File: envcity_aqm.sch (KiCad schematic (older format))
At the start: 9 parts, among them Q1 BSS138, Q2 BSS138, Q3 BSS138

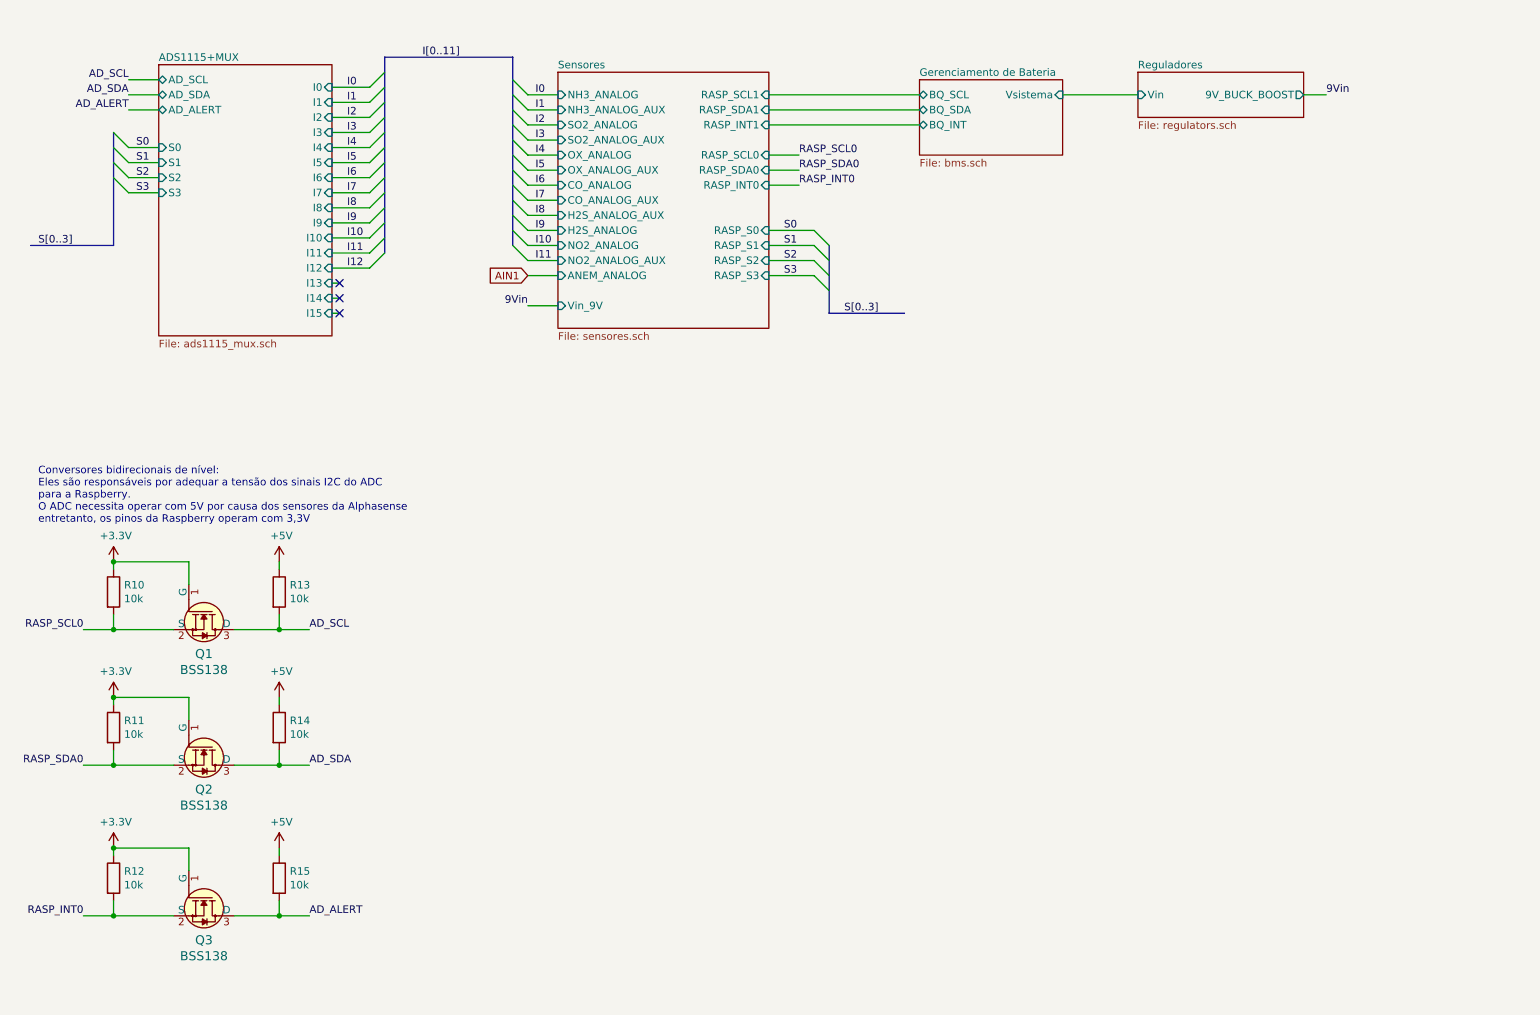
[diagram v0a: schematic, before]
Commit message: Adicionando radio LoRa. Criando um .sch para a Raspberry e para o radio
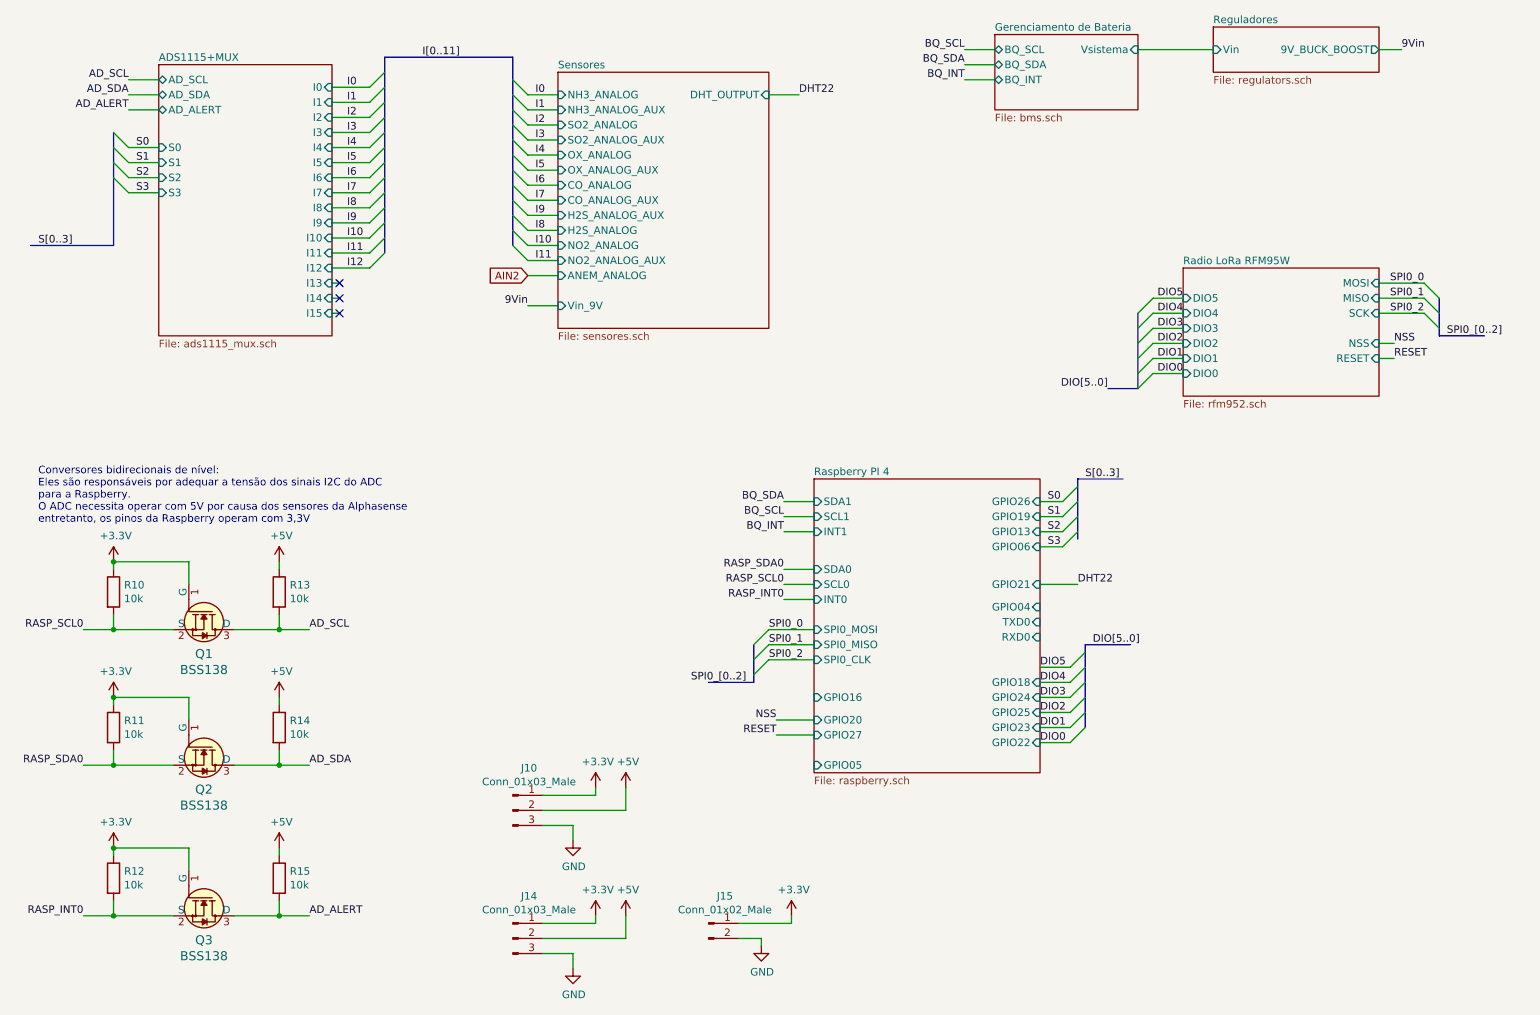
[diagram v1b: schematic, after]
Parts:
- added J10, J14: Conn_01x03_Male, Connector_PinHeader_2.54mm:PinHeader_1x03_P2.54mm_Vertical, symbol Connector:Conn_01x03_Male
- added J15: Conn_01x02_Male, Connector_PinSocket_2.54mm:PinSocket_1x02_P2.54mm_Vertical, symbol Connector:Conn_01x02_Male
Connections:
- net +3V3: now also J10.1 (Pin_1), J14.1 (Pin_1), J15.1 (Pin_1)
- net +5V: now also J10.2 (Pin_2), J14.2 (Pin_2)
- new net GND: J10.3 (Pin_3), J14.3 (Pin_3), J15.2 (Pin_2)

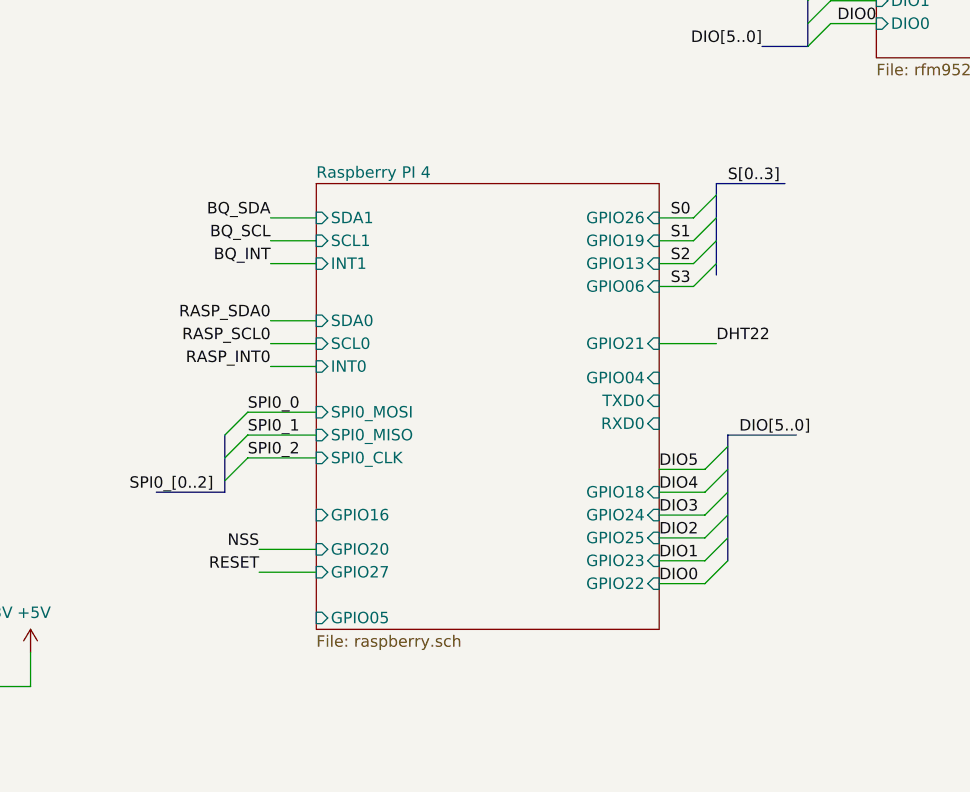
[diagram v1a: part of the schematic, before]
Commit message: Versão v0 finalizada. Adiciona pasta para os arquivos de saída e de fabricacao.
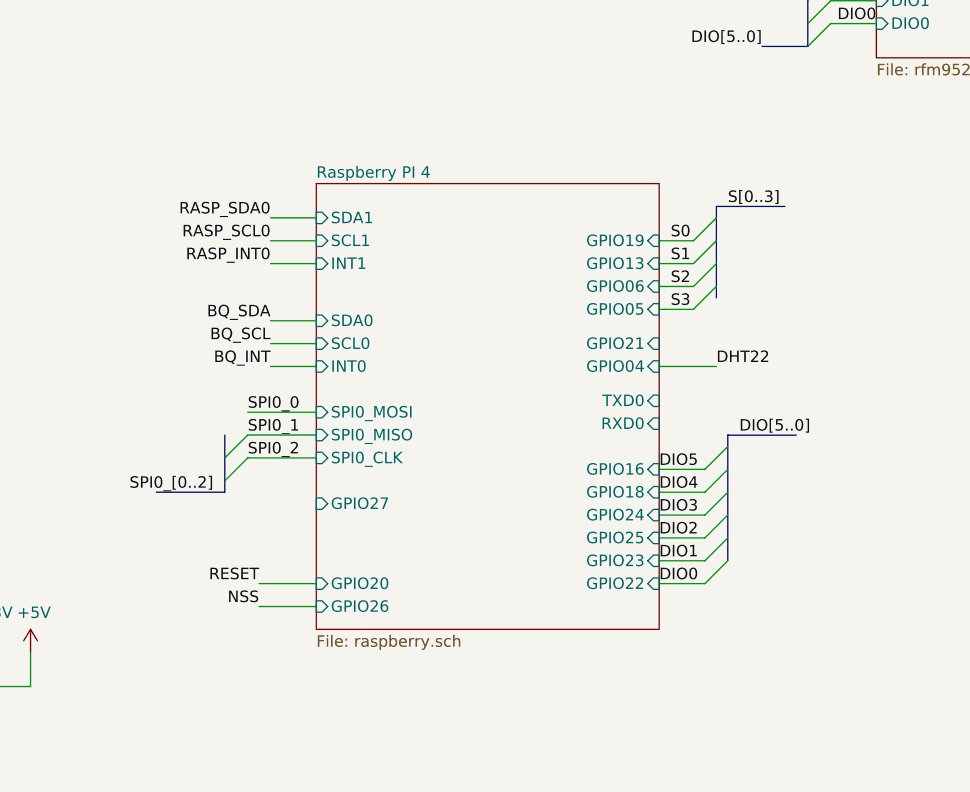
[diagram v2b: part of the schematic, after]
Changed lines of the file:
@@
 Wire Wire Line
 	2100 1750 1900 1750
-Entry Wire Line
-	8100 4100 8200 4000
-Entry Wire Line
-	8100 4200 8200 4100
-Entry Wire Line
-	8100 4300 8200 4200
-Entry Wire Line
-	8100 4400 8200 4300
-Wire Wire Line
-	7950 4100 8100 4100
-Wire Wire Line
-	7950 4200 8100 4200
-Wire Wire Line
-	7950 4300 8100 4300
-Wire Wire Line
-	7950 4400 8100 4400
-Text Label 8000 4100 0    50   ~ 0
-S0
-Text Label 8000 4200 0    50   ~ 0
-S1
-Text Label 8000 4300 0    50   ~ 0
-S2
-Text Label 8000 4400 0    50   ~ 0
-S3
 Wire Wire Line
 	6450 4100 6250 4100
@@
 Wire Wire Line
 	6450 4300 6250 4300
-Text Label 6250 4650 2    50   ~ 0
+Text Label 6250 4200 2    50   ~ 0
 RASP_SCL0
-Text Label 6250 4550 2    50   ~ 0
+Text Label 6250 4100 2    50   ~ 0
 RASP_SDA0
-Text Label 6250 4750 2    50   ~ 0
+Text Label 6250 4300 2    50   ~ 0
 RASP_INT0
-Wire Bus Line
-	8200 3950 8500 3950
 Wire Wire Line
 	7650 1100 7450 1100
@@
 Wire Wire Line
 	6450 4750 6250 4750
-Text Label 6250 4100 2    50   ~ 0
+Text Label 6250 4550 2    50   ~ 0
 BQ_SDA
-Text Label 6250 4200 2    50   ~ 0
+Text Label 6250 4650 2    50   ~ 0
 BQ_SCL
-Text Label 6250 4300 2    50   ~ 0
+Text Label 6250 4750 2    50   ~ 0
 BQ_INT
-Entry Wire Line
-	6150 4950 6050 5050
 Entry Wire Line
 	6050 5150 6150 5050
@@
 DHT22
 Wire Wire Line
-	7950 4650 8200 4650
-Text Label 8200 4650 0    50   ~ 0
+	7950 4750 8200 4750
+Text Label 8200 4750 0    50   ~ 0
 DHT22
 $Sheet
@@
 Text Label 8900 3250 2    50   ~ 0
 DIO0
-Text Label 8250 3950 0    50   ~ 0
-S[0..3]
 Wire Wire Line
 	8700 2750 8900 2750
@@
 Text Label 10300 3150 0    50   ~ 0
 RESET
-Text Label 6200 5550 2    50   ~ 0
+Text Label 6200 5800 2    50   ~ 0
 NSS
-Text Label 6200 5650 2    50   ~ 0
+Text Label 6200 5700 2    50   ~ 0
 RESET
 Wire Wire Line
-	6450 5550 6200 5550
-Wire Wire Line
-	6450 5650 6200 5650
+	6450 5700 6200 5700
+Wire Wire Line
+	6450 5800 6200 5800
 $Comp
 L Connector:Conn_01x03_Male J10
@@
 F6 "SDA0" I L 6450 4550 50
 F7 "INT0" I L 6450 4750 50
-F8 "GPIO20" I L 6450 5550 50
+F8 "GPIO20" I L 6450 5700 50
 F9 "SPI0_MOSI" I L 6450 4950 50
 F10 "SPI0_MISO" I L 6450 5050 50
@@
 F12 "TXD0" I R 7950 4900 50
 F13 "RXD0" I R 7950 5000 50
-F14 "GPIO27" I L 6450 5650 50
+F14 "GPIO27" I L 6450 5350 50
 F15 "GPIO18" I R 7950 5300 50
 F16 "GPIO24" I R 7950 5400 50
 F17 "GPIO25" I R 7950 5500 50
-F18 "GPIO26" I R 7950 4100 50
+F18 "GPIO26" I L 6450 5800 50
 F19 "GPIO22" I R 7950 5700 50
 F20 "GPIO21" I R 7950 4650 50
 F21 "GPIO13" I R 7950 4300 50
-F22 "GPIO04" I R 7950 4800 50
-F23 "GPIO16" I L 6450 5400 50
+F22 "GPIO04" I R 7950 4750 50
+F23 "GPIO16" I R 7950 5200 50
 F24 "GPIO19" I R 7950 4200 50
 F25 "GPIO23" I R 7950 5600 50
-F26 "GPIO05" I L 6450 5850 50
+F26 "GPIO05" I R 7950 4500 50
 F27 "GPIO06" I R 7950 4400 50
 $EndSheet
+Text Label 8250 4050 0    50   ~ 0
+S[0..3]
+Wire Bus Line
+	8200 4050 8500 4050
+Text Label 8000 4500 0    50   ~ 0
+S3
+Text Label 8000 4400 0    50   ~ 0
+S2
+Text Label 8000 4300 0    50   ~ 0
+S1
+Text Label 8000 4200 0    50   ~ 0
+S0
+Wire Wire Line
+	7950 4500 8100 4500
+Wire Wire Line
+	7950 4400 8100 4400
+Wire Wire Line
+	7950 4300 8100 4300
+Wire Wire Line
+	7950 4200 8100 4200
+Entry Wire Line
+	8100 4500 8200 4400
+Entry Wire Line
+	8100 4400 8200 4300
+Entry Wire Line
+	8100 4300 8200 4200
+Entry Wire Line
+	8100 4200 8200 4100
 Wire Bus Line
 	6050 5050 6050 5300
@@
 	8600 2850 8600 3350
 Wire Bus Line
-	8200 3950 8200 4350
-Wire Bus Line
 	1800 1650 1800 2400
 Wire Bus Line
 	8250 5050 8250 5600
 Wire Bus Line
+	8200 4050 8200 4450
+Wire Bus Line
 	4450 1150 4450 2400
